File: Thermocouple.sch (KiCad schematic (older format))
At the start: 0 parts

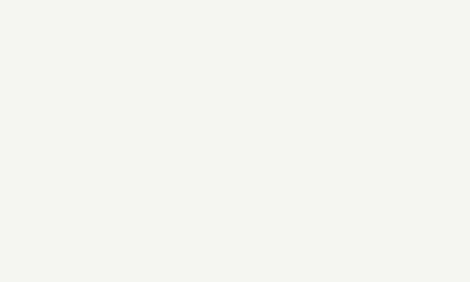
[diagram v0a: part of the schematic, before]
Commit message: Created inputs/outputs in hierarchical sheets
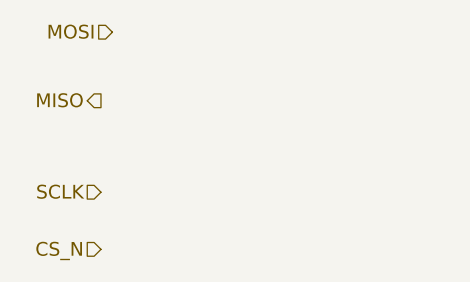
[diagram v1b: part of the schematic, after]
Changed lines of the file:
@@
 Text HLabel 8050 2550 2    60   Input ~ 0
 TC_IN_-
+Text HLabel 2300 1750 0    60   Input ~ 0
+MOSI
+Text HLabel 2250 2050 0    60   Output ~ 0
+MISO
+Text HLabel 2250 2450 0    60   Input ~ 0
+SCLK
+Text HLabel 2250 2700 0    60   Input ~ 0
+CS_N
 $EndSCHEMATC

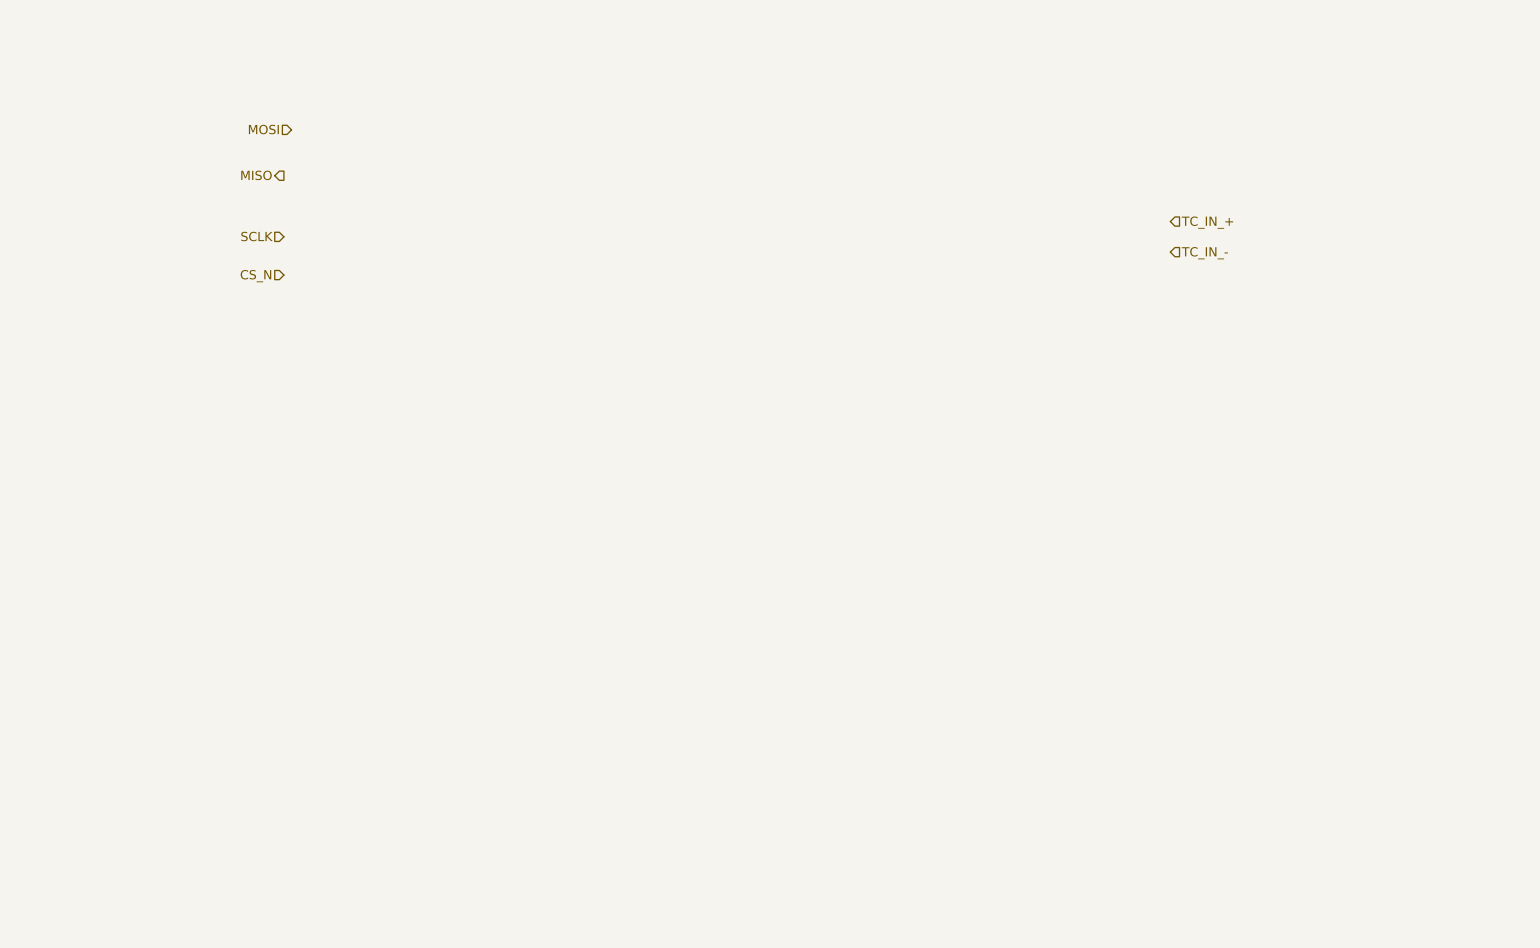
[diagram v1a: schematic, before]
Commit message: Created first schematic for Thermocouple module
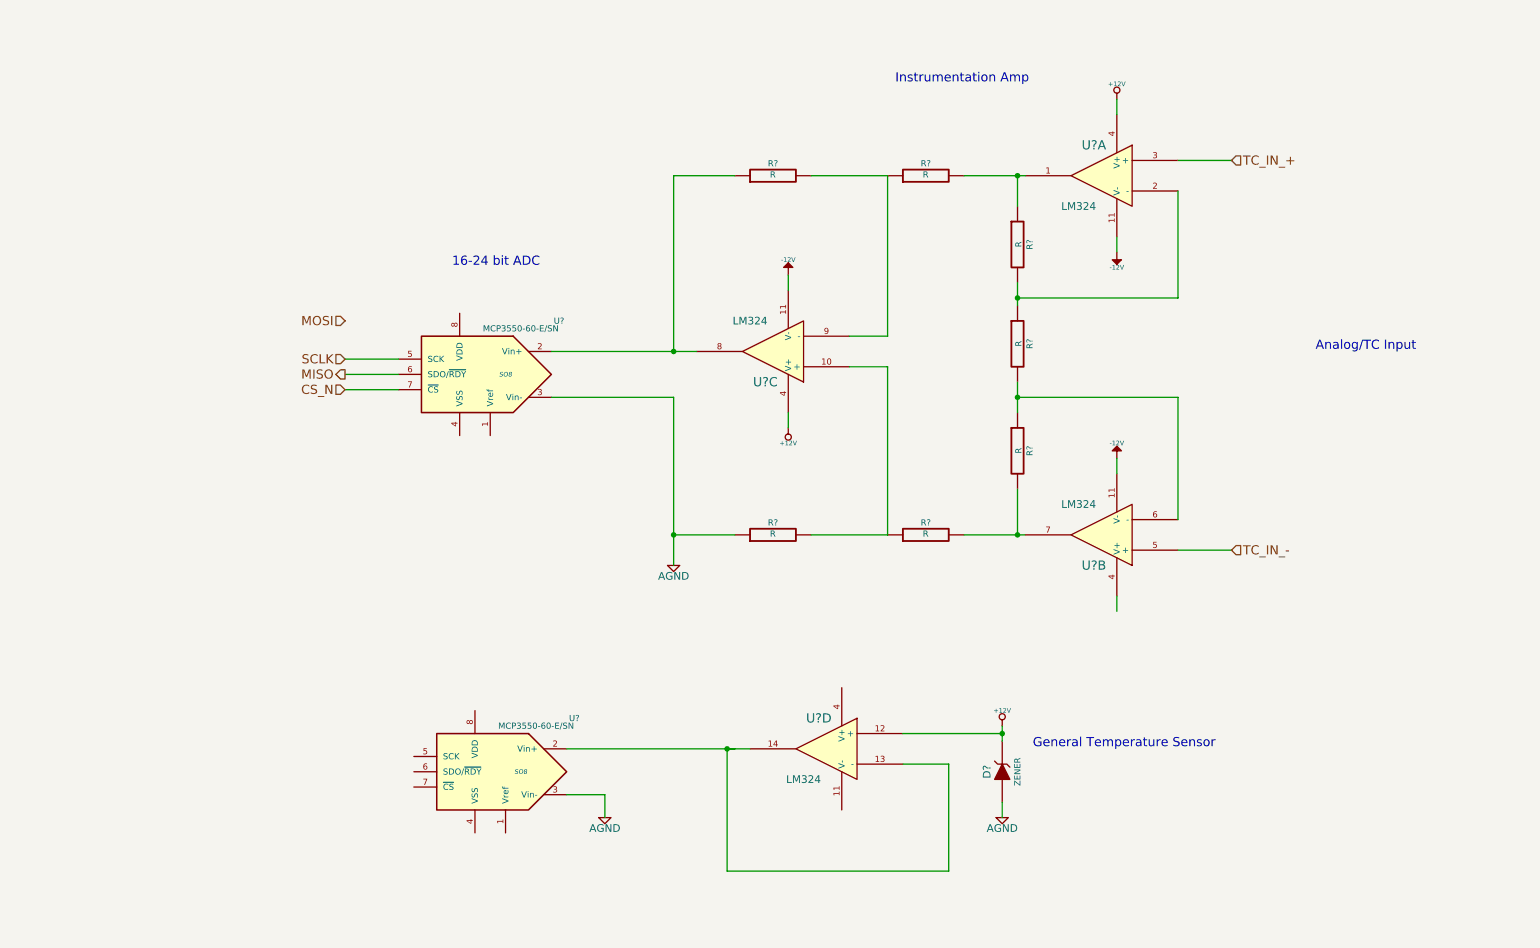
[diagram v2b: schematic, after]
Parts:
- added D?: ZENER, ~, symbol ZENER
- added R? (x7): R, ~, symbol R
- added U? (x4): LM324, ~, symbol LM324
- added U? (x2): MCP3550-60-E/SN, SO8, symbol MCP3550-60-E/SN
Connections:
- net CS_N: now also U?.7 (~CS~)
- net MISO: now also U?.6 (SDO/~RDY~)
- net SCLK: now also U?.5 (SCK)
- net TC_IN_+: now also U?.3 (+)
- net TC_IN_-: now also U?.5 (+)
- new net: R?.1, R?.2, U?.1
- new net: R?.1, R?.2, U?.2 (-)
- new net: R?.1, R?.2, U?.6 (-)
- new net: R?.2, R?.2, U?.7
- new net: R?.1, R?.2, U?.10 (+)
- new net: R?.1, U?.2 (Vin+), U?.8
- new net: R?.1, R?.2, U?.9 (-)
- new net: U?.13 (-), U?.14, U?.2 (Vin+)
- new net +12V: D?.2 (K), U?.12 (+), U?.4 (V+), U?.4 (V+)
- new net -12V: U?.11 (V-), U?.11 (V-), U?.11 (V-)
- new net AGND: D?.1 (A), R?.1, U?.3 (Vin-), U?.3 (Vin-)
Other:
- note added: "16-24 bit ADC"
- note added: "Analog/TC Input"
- note added: "General Temperature Sensor"
- note added: "Instrumentation Amp"

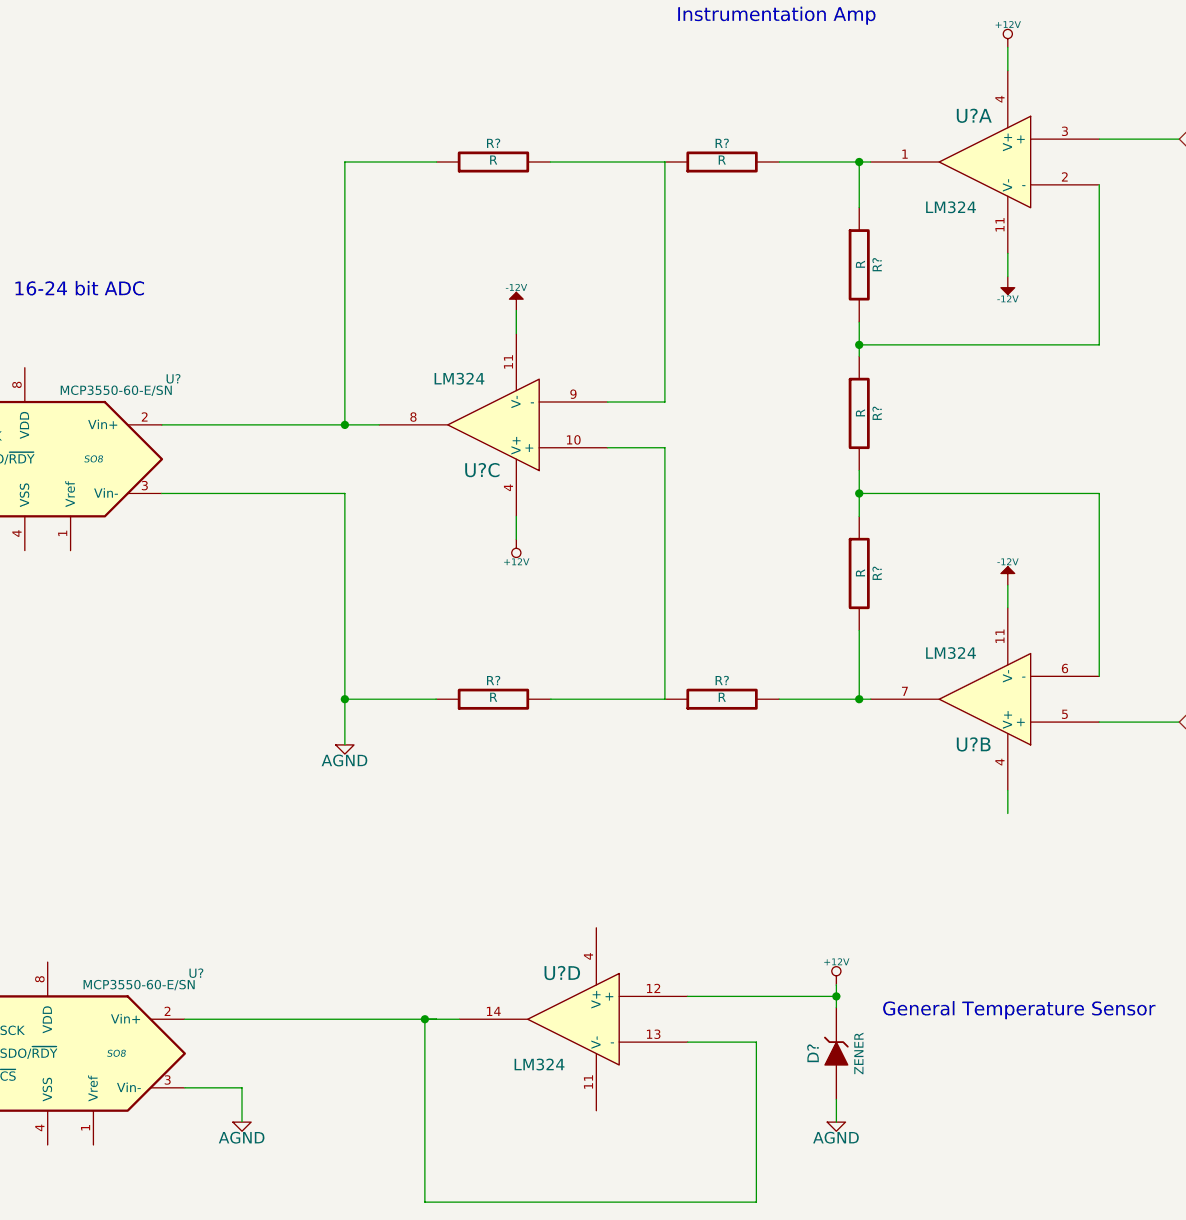
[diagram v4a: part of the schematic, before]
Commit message: Created the first schematic in both Power modules
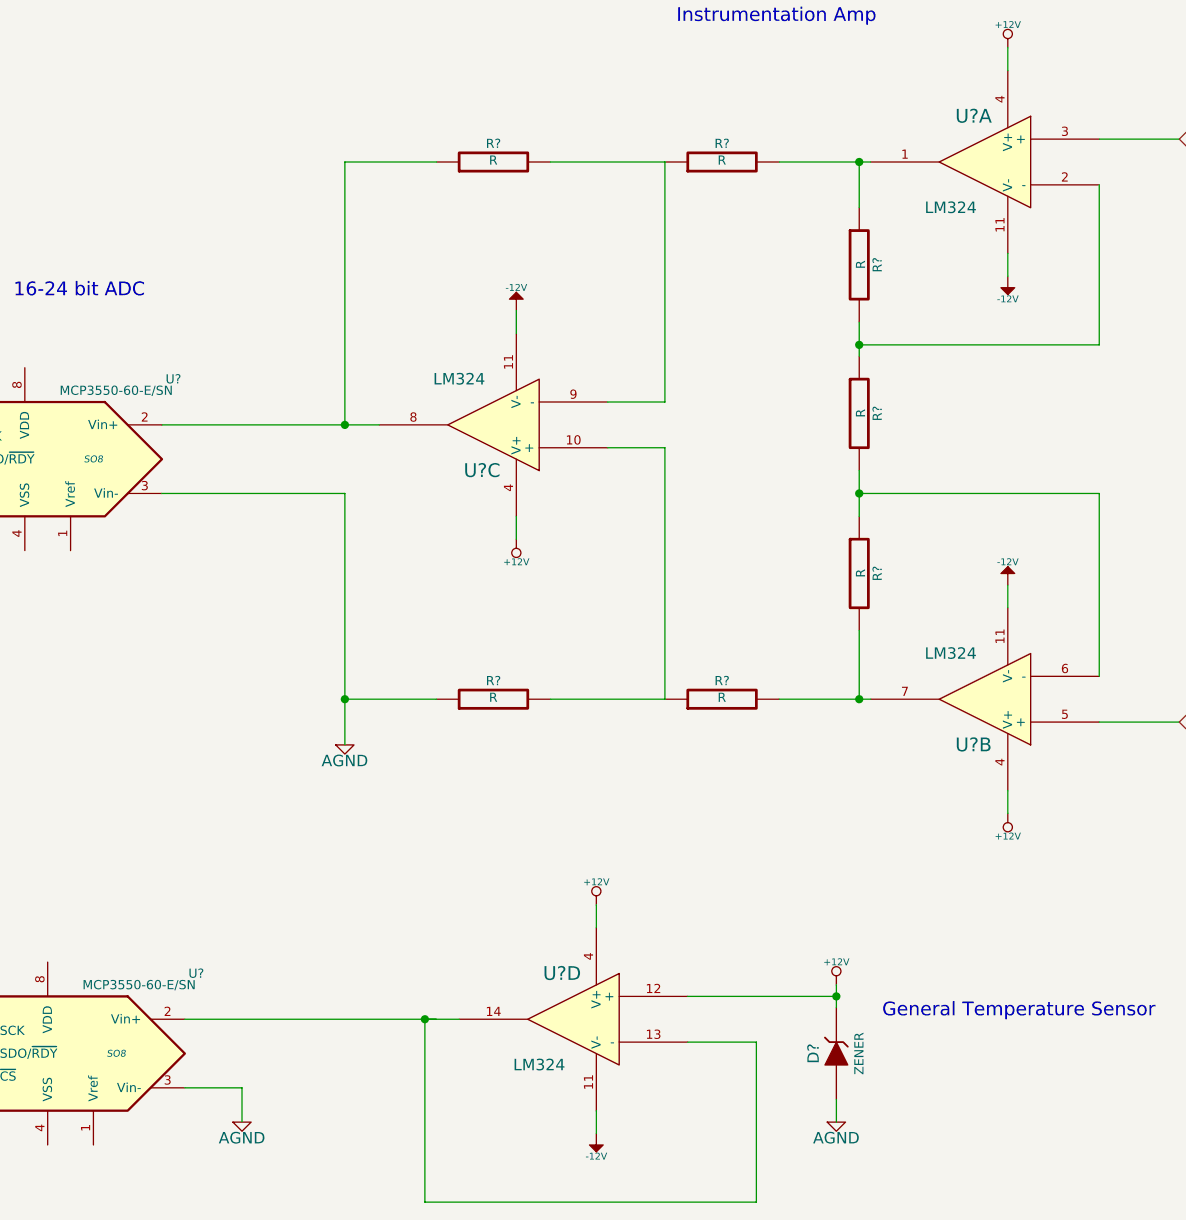
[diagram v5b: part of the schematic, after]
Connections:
- net +12V: now also U?.4 (V+), U?.4 (V+)
- net -12V: now also U?.11 (V-)
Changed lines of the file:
@@
 $Descr A4 11693 8268
 encoding utf-8
-Sheet 3 8
+Sheet 3 9
 Title ""
-Date "9 feb 2014"
+Date "10 feb 2014"
 Rev ""
 Comp ""
@@
 	7050 4100 7050 4400
 Wire Wire Line
-	6700 4400 7050 4400
-Wire Wire Line
-	7050 4400 7100 4400
-Wire Wire Line
-	7050 3400 7050 3500
-Wire Wire Line
-	7050 3500 7050 3600
-Wire Wire Line
-	7050 2750 7050 2850
-Wire Wire Line
-	7050 2850 7050 2900
+	6700 4400 7100 4400
+Wire Wire Line
+	7050 3400 7050 3600
+Wire Wire Line
+	7050 2750 7050 2900
 Wire Wire Line
 	7050 2250 7050 2050
 Wire Wire Line
-	6700 2050 7050 2050
-Wire Wire Line
-	7050 2050 7100 2050
+	6700 2050 7100 2050
 Wire Wire Line
 	7050 2850 8100 2850
@@
 	4800 2050 4800 3200
 Wire Wire Line
-	4000 3200 4800 3200
-Wire Wire Line
-	4800 3200 4950 3200
+	4000 3200 4950 3200
 Wire Wire Line
 	6200 4400 5700 4400
@@
 $EndComp
 Wire Wire Line
-	4800 3500 4800 4400
-Wire Wire Line
-	4800 4400 4800 4600
+	4800 3500 4800 4600
 Wire Wire Line
 	4800 4400 5200 4400
@@
 $EndComp
 Wire Wire Line
-	6950 5650 6950 5700
-Wire Wire Line
-	6950 5700 6950 5750
+	6950 5650 6950 5750
 $Comp
 L AGND #PWR?
@@
 	5150 6600 5150 5800
 Wire Wire Line
-	5150 5800 5200 5800
-Wire Wire Line
-	5200 5800 5300 5800
+	5150 5800 5300 5800
 $Comp
 L MCP3550-60-E/SN U?
@@
 Text Notes 3350 2650 0    60   ~ 0
 16-24 bit ADC
+$Comp
+L +12V #PWR?
+U 1 1 52F82613
+P 7700 4900
+F 0 "#PWR?" H 7700 4850 20  0001 C CNN
+F 1 "+12V" H 7700 5000 30  0000 C CNN
+F 2 "" H 7700 4900 60  0000 C CNN
+F 3 "" H 7700 4900 60  0000 C CNN
+	1    7700 4900
+	-1   0    0    1
+$EndComp
+$Comp
+L +12V #PWR?
+U 1 1 52F827D8
+P 5900 5300
+F 0 "#PWR?" H 5900 5250 20  0001 C CNN
+F 1 "+12V" H 5900 5400 30  0000 C CNN
+F 2 "" H 5900 5300 60  0000 C CNN
+F 3 "" H 5900 5300 60  0000 C CNN
+	1    5900 5300
+	1    0    0    -1
+$EndComp
+$Comp
+L -12V #PWR?
+U 1 1 52F827DE
+P 5900 6300
+F 0 "#PWR?" H 5900 6430 20  0001 C CNN
+F 1 "-12V" H 5900 6400 30  0000 C CNN
+F 2 "" H 5900 6300 60  0000 C CNN
+F 3 "" H 5900 6300 60  0000 C CNN
+	1    5900 6300
+	-1   0    0    1
+$EndComp
+Wire Wire Line
+	5900 6200 5900 6300
+Wire Wire Line
+	5900 5300 5900 5400
 $EndSCHEMATC
